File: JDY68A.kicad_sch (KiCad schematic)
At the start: 7 parts, among them U9 PAM8302AAS

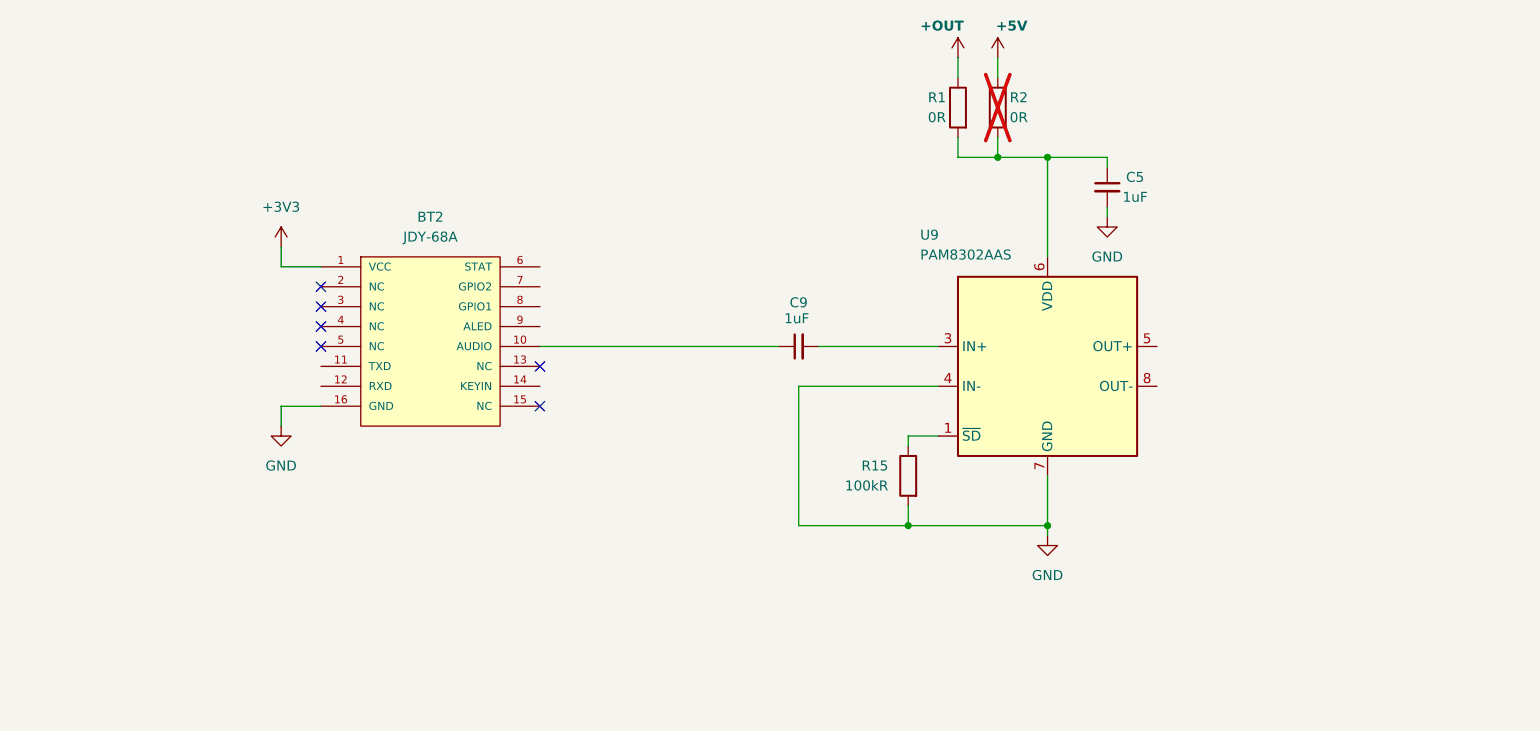
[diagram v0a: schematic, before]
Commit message: Changed LDO to Buc-Boost
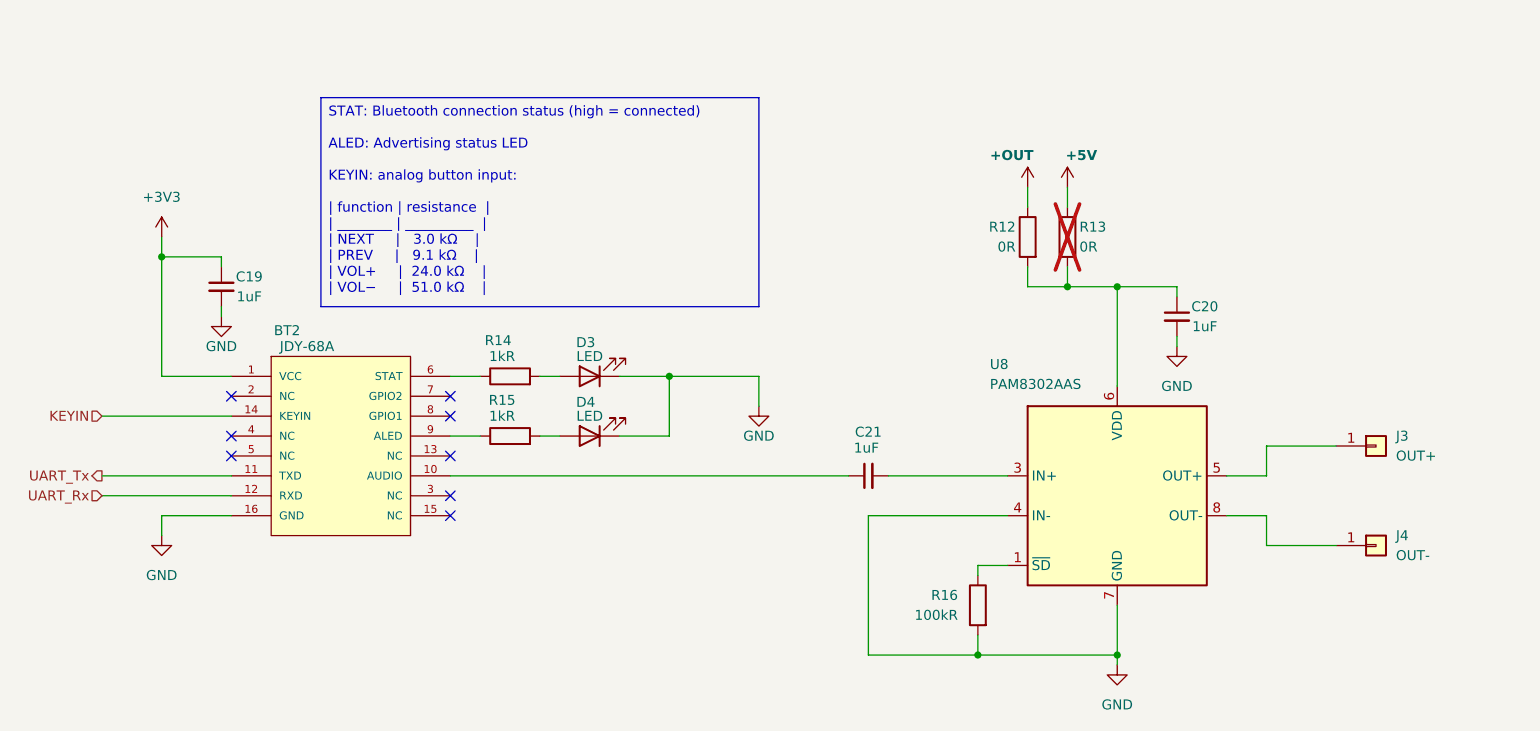
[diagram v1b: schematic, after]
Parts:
- added C19: 1uF, Capacitor_SMD:C_0805_2012Metric_Pad1.18x1.45mm_HandSolder, symbol Device:C_Small
- added D3, D4: LED, LED_SMD:LED_0805_2012Metric_Pad1.15x1.40mm_HandSolder, symbol Device:LED
- added J3: OUT+, Connector_PinSocket_2.54mm:PinSocket_1x01_P2.54mm_Vertical, symbol Connector_Generic:Conn_01x01
- added J4: OUT-, Connector_PinSocket_2.54mm:PinSocket_1x01_P2.54mm_Vertical, symbol Connector_Generic:Conn_01x01
- added R14, R15: 1kR, Resistor_SMD:R_0805_2012Metric_Pad1.20x1.40mm_HandSolder, symbol Device:R
- C20: renamed from C5; footprint (none) -> Capacitor_SMD:C_0805_2012Metric_Pad1.18x1.45mm_HandSolder
- C21: renamed from C9; footprint (none) -> Capacitor_SMD:C_0805_2012Metric_Pad1.18x1.45mm_HandSolder
- R12: renamed from R1; footprint (none) -> Resistor_SMD:R_0805_2012Metric_Pad1.20x1.40mm_HandSolder
- R13: renamed from R2; footprint (none) -> Resistor_SMD:R_0805_2012Metric_Pad1.20x1.40mm_HandSolder
- R16: renamed from R15; footprint (none) -> Resistor_SMD:R_0805_2012Metric_Pad1.20x1.40mm_HandSolder
- renumbered U9 to U8
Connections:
- net +3V3: now also C19.1
- net GND: now also C19.2, D3.1 (K), D4.1 (K)
- net at U8.5 (OUT+): now also J3.1 (Pin_1)
- net at U8.8 (OUT-): now also J4.1 (Pin_1)
- net UART_Tx: now reaches BT2.11 (TXD)
- net UART_Rx: now reaches BT2.12 (RXD)
- net KEYIN: now reaches BT2.14 (KEYIN)
- net at BT2.6 (STAT): now also R14.1
- net at BT2.9 (ALED): now also R15.1
- new net: D4.2 (A), R15.2
- new net: D3.2 (A), R14.2
- no-connect marks 6 -> 8
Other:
- moved on the sheet: BT2, C20, C21, R12, R13, R16, U8

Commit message: Added LEDs + TPs
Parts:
- BT2: footprint (none) -> JDY68A:JDY-68A_Module
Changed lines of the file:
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@@
 			)
 		)
-		(property "Footprint" ""
+		(property "Footprint" "JDY68A:JDY-68A_Module"
 			(at 91.44 78.74 0)
 			(effects

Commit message: Added layout
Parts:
- added C25: 10uF, Capacitor_SMD:C_0805_2012Metric_Pad1.18x1.45mm_HandSolder, symbol Device:C_Small
- added R24, R25: 10kR, Resistor_SMD:R_0805_2012Metric_Pad1.20x1.40mm_HandSolder, symbol Device:R
- added R26: 100kR, Resistor_SMD:R_0805_2012Metric_Pad1.20x1.40mm_HandSolder, symbol Device:R
- C21: value 1uF -> 10uF
- J3, J4: footprint Connector_PinSocket_2.54mm:PinSocket_1x01_P2.54mm_Vertical -> Connector_PinHeader_2.54mm:PinHeader_1x01_P2.54mm_Vertical
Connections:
- net GND: now also R26.1
- net at U8.3 (IN+): now also R24.2, R25.2, R26.2; no longer C21.2
- new net: C25.2, R25.1
- new net: C21.2, R24.1
- new net MCU_AUDIO: C25.1
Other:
- moved on the sheet: C21

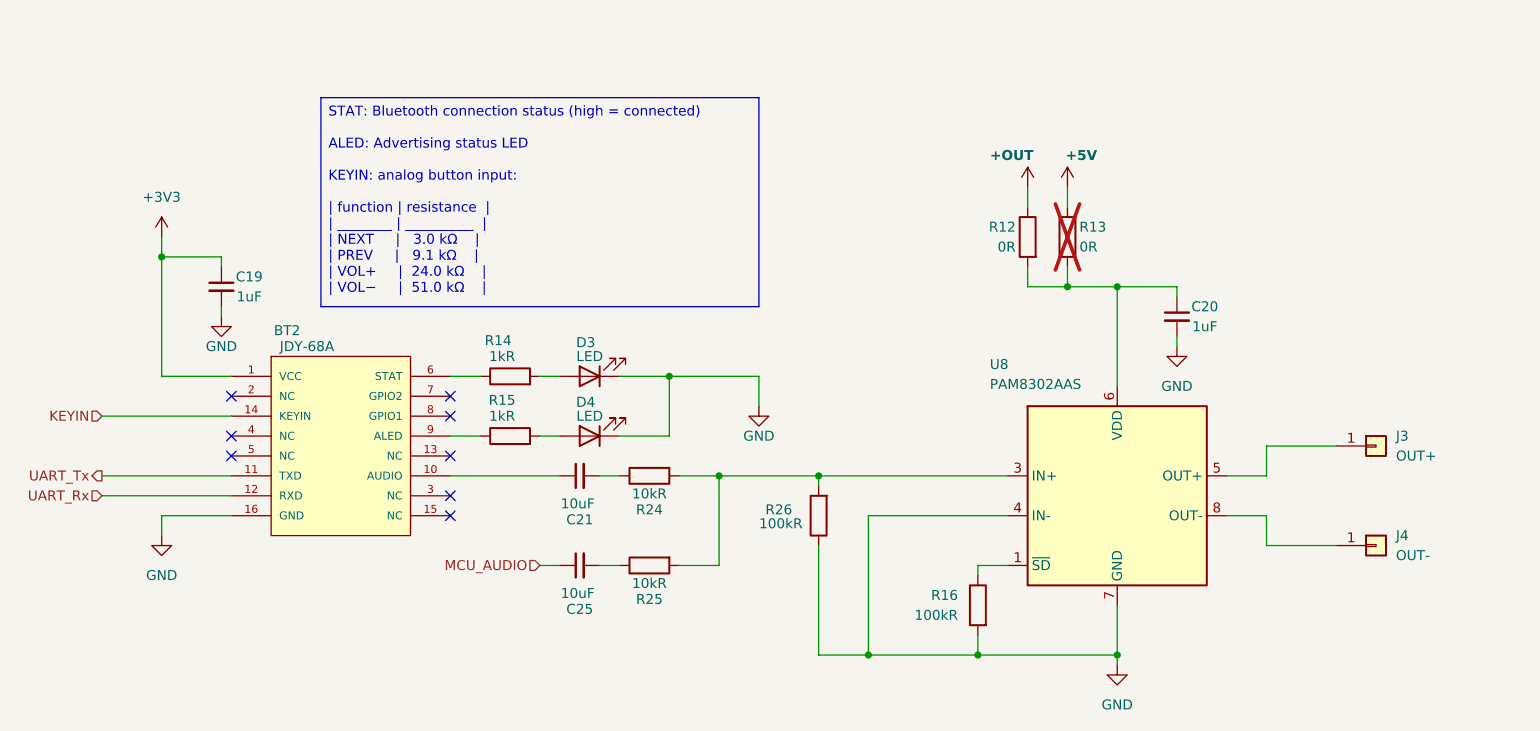
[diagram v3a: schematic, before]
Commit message: Did Silkscreen + added images of PCBA
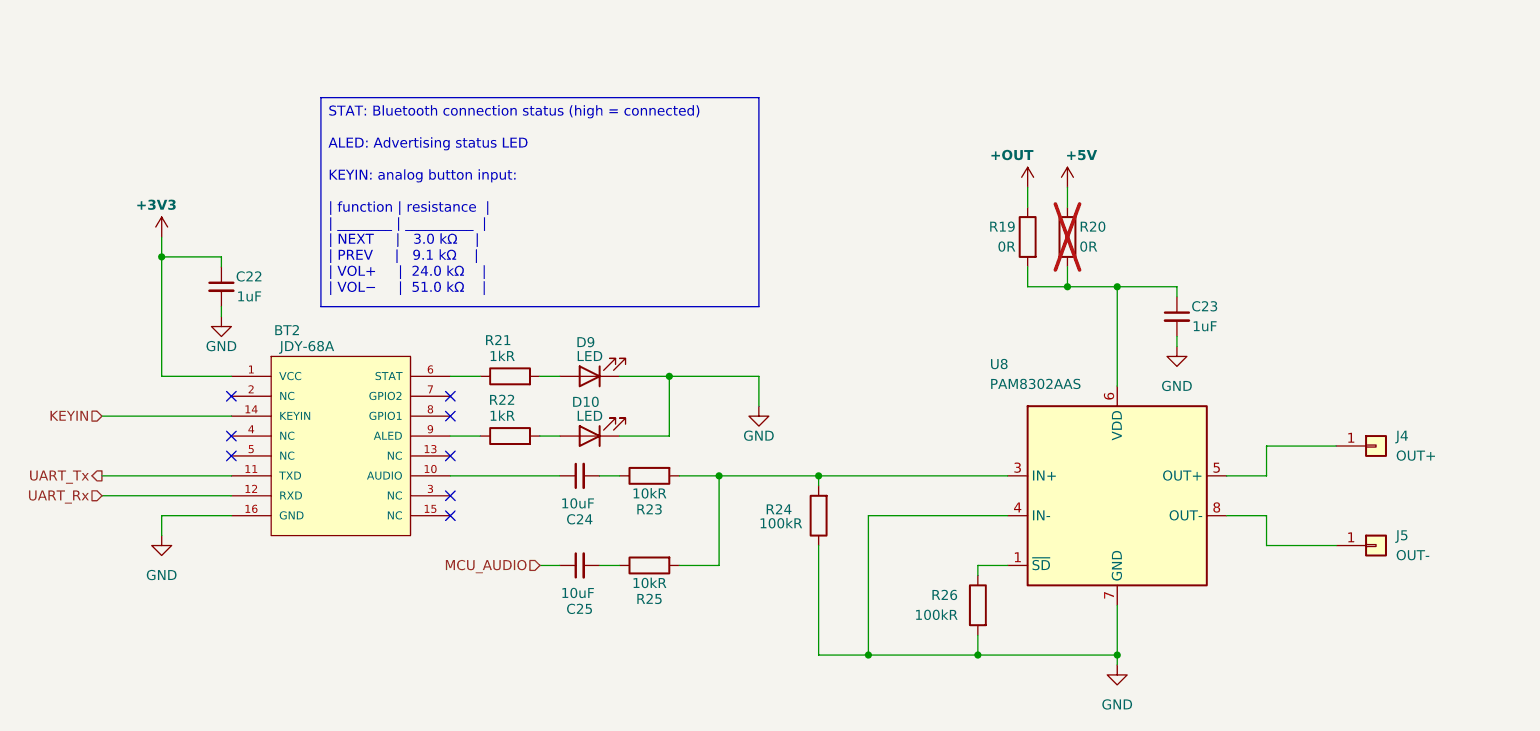
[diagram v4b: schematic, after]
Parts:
- renumbered C19 to C22, C20 to C23, C21 to C24, D4 to D10, D3 to D9, J3 to J4, J4 to J5, R12 to R19, R13 to R20, R14 to R21, R15 to R22, R24 to R23, R26 to R24, R16 to R26
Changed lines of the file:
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@@
 	(title_block
 		(title "Snail v1")
-		(date "2026-03-29")
+		(date "2026-04-06")
 		(company "Author: Christian R")
 	)
@@
 		(on_board yes)
 		(dnp no)
-		(property "Reference" "R15"
+		(property "Reference" "R22"
 			(at 112.014 83.058 90)
 			(effects
@@
 			(project "Snail_v1"
 				(path "/98695d9f-8521-4f7d-bb41-f22c1215a8e7/d0e1ba84-93bf-4c92-b310-ee99f2c34828"
-					(reference "R15")
+					(reference "R22")
 					(unit 1)
 				)
@@
 		(dnp no)
 		(fields_autoplaced yes)
-		(property "Reference" "#PWR032"
+		(property "Reference" "#PWR044"
 			(at 198.12 82.55 0)
 			(effects
@@
 			(project "Snail_v1"
 				(path "/98695d9f-8521-4f7d-bb41-f22c1215a8e7/d0e1ba84-93bf-4c92-b310-ee99f2c34828"
-					(reference "#PWR032")
+					(reference "#PWR044")
 					(unit 1)
 				)
@@
 		(on_board yes)
 		(dnp no)
-		(property "Reference" "#PWR031"
+		(property "Reference" "#PWR043"
 			(at 76.2 78.74 0)
 			(effects
@@
 			(project "Snail_v1"
 				(path "/98695d9f-8521-4f7d-bb41-f22c1215a8e7/d0e1ba84-93bf-4c92-b310-ee99f2c34828"
-					(reference "#PWR031")
+					(reference "#PWR043")
 					(unit 1)
 				)
@@
 		(on_board yes)
 		(dnp no)
-		(property "Reference" "D3"
+		(property "Reference" "D9"
 			(at 122.682 75.692 0)
 			(effects
@@
 			(project ""
 				(path "/98695d9f-8521-4f7d-bb41-f22c1215a8e7/d0e1ba84-93bf-4c92-b310-ee99f2c34828"
-					(reference "D3")
+					(reference "D9")
 					(unit 1)
 				)
@@
 		(on_board yes)
 		(dnp no)
-		(property "Reference" "D4"
+		(property "Reference" "D10"
 			(at 122.682 83.312 0)
 			(effects
@@
 			(project "Snail_v1"
 				(path "/98695d9f-8521-4f7d-bb41-f22c1215a8e7/d0e1ba84-93bf-4c92-b310-ee99f2c34828"
-					(reference "D4")
+					(reference "D10")
 					(unit 1)
 				)
@@
 		(on_board yes)
 		(dnp no)
-		(property "Reference" "R14"
+		(property "Reference" "R21"
 			(at 111.506 75.438 90)
 			(effects
@@
 			(project ""
 				(path "/98695d9f-8521-4f7d-bb41-f22c1215a8e7/d0e1ba84-93bf-4c92-b310-ee99f2c34828"
-					(reference "R14")
+					(reference "R21")
 					(unit 1)
 				)
@@
 		(on_board yes)
 		(dnp no)
-		(property "Reference" "C20"
+		(property "Reference" "C23"
 			(at 201.676 71.12 0)
 			(effects
@@
 			(project "Snail_v1"
 				(path "/98695d9f-8521-4f7d-bb41-f22c1215a8e7/d0e1ba84-93bf-4c92-b310-ee99f2c34828"
-					(reference "C20")
+					(reference "C23")
 					(unit 1)
 				)
@@
 		(on_board yes)
 		(dnp no)
-		(property "Reference" "R24"
+		(property "Reference" "R23"
 			(at 130.81 97.028 90)
 			(effects
@@
 			(project "Snail_v1"
 				(path "/98695d9f-8521-4f7d-bb41-f22c1215a8e7/d0e1ba84-93bf-4c92-b310-ee99f2c34828"
-					(reference "R24")
+					(reference "R23")
 					(unit 1)
 				)
@@
 		(on_board yes)
 		(dnp no)
-		(property "Reference" "#PWR029"
+		(property "Reference" "#PWR041"
 			(at 184.15 59.69 0)
 			(effects
@@
 			(project "Snail_v1"
 				(path "/98695d9f-8521-4f7d-bb41-f22c1215a8e7/d0e1ba84-93bf-4c92-b310-ee99f2c34828"
-					(reference "#PWR029")
+					(reference "#PWR041")
 					(unit 1)
 				)
@@
 		(on_board yes)
 		(dnp no)
-		(property "Reference" "R26"
+		(property "Reference" "R24"
 			(at 147.32 97.028 0)
 			(effects
@@
 			(project "Snail_v1"
 				(path "/98695d9f-8521-4f7d-bb41-f22c1215a8e7/d0e1ba84-93bf-4c92-b310-ee99f2c34828"
-					(reference "R26")
+					(reference "R24")
 					(unit 1)
 				)
@@
 		(dnp no)
 		(fields_autoplaced yes)
-		(property "Reference" "J3"
+		(property "Reference" "J4"
 			(at 226.06 87.6299 0)
 			(effects
@@
 			(project ""
 				(path "/98695d9f-8521-4f7d-bb41-f22c1215a8e7/d0e1ba84-93bf-4c92-b310-ee99f2c34828"
-					(reference "J3")
+					(reference "J4")
 					(unit 1)
 				)
@@
 		(on_board yes)
 		(dnp no)
-		(property "Reference" "C19"
+		(property "Reference" "C22"
 			(at 79.756 67.31 0)
 			(effects
@@
 			(project "Snail_v1"
 				(path "/98695d9f-8521-4f7d-bb41-f22c1215a8e7/d0e1ba84-93bf-4c92-b310-ee99f2c34828"
-					(reference "C19")
+					(reference "C22")
 					(unit 1)
 				)
@@
 		(on_board yes)
 		(dnp no)
-		(fields_autoplaced yes)
-		(property "Reference" "#PWR030"
+		(property "Reference" "#PWR042"
 			(at 68.58 66.04 0)
 			(effects
@@
 		)
 		(property "Value" "+3V3"
-			(at 68.58 57.15 0)
-			(effects
-				(font
-					(size 1.27 1.27)
-				)
+			(at 65.278 58.166 0)
+			(effects
+				(font
+					(size 1.27 1.27)
+					(thickness 0.254)
+					(bold yes)
+					(color 255 0 0 1)
+				)
+				(justify left)
 			)
 		)
@@
 			(project ""
 				(path "/98695d9f-8521-4f7d-bb41-f22c1215a8e7/d0e1ba84-93bf-4c92-b310-ee99f2c34828"
-					(reference "#PWR030")
+					(reference "#PWR042")
 					(unit 1)
 				)
@@
 		(on_board yes)
 		(dnp no)
-		(property "Reference" "R12"
+		(property "Reference" "R19"
 			(at 177.546 60.96 0)
 			(effects
@@
 			(project "Snail_v1"
 				(path "/98695d9f-8521-4f7d-bb41-f22c1215a8e7/d0e1ba84-93bf-4c92-b310-ee99f2c34828"
-					(reference "R12")
+					(reference "R19")
 					(unit 1)
 				)
@@
 		(on_board yes)
 		(dnp no)
-		(property "Reference" "R16"
+		(property "Reference" "R26"
 			(at 170.18 107.9499 0)
 			(effects
@@
 			(project "Snail_v1"
 				(path "/98695d9f-8521-4f7d-bb41-f22c1215a8e7/d0e1ba84-93bf-4c92-b310-ee99f2c34828"
-					(reference "R16")
+					(reference "R26")
 					(unit 1)
 				)
@@
 		(on_board yes)
 		(dnp yes)
-		(property "Reference" "R13"
+		(property "Reference" "R20"
 			(at 185.674 60.96 0)
 			(effects
@@
 			(project "Snail_v1"
 				(path "/98695d9f-8521-4f7d-bb41-f22c1215a8e7/d0e1ba84-93bf-4c92-b310-ee99f2c34828"
-					(reference "R13")
+					(reference "R20")
 					(unit 1)
 				)
@@
 		(dnp no)
 		(fields_autoplaced yes)
-		(property "Reference" "#PWR035"
+		(property "Reference" "#PWR047"
 			(at 190.5 123.19 0)
 			(effects
@@
 			(project "Snail_v1"
 				(path "/98695d9f-8521-4f7d-bb41-f22c1215a8e7/d0e1ba84-93bf-4c92-b310-ee99f2c34828"
-					(reference "#PWR035")
+					(reference "#PWR047")
 					(unit 1)
 				)
@@
 		(dnp no)
 		(fields_autoplaced yes)
-		(property "Reference" "J4"
+		(property "Reference" "J5"
 			(at 226.06 100.3299 0)
 			(effects
@@
 			(project "Snail_v1"
 				(path "/98695d9f-8521-4f7d-bb41-f22c1215a8e7/d0e1ba84-93bf-4c92-b310-ee99f2c34828"
-					(reference "J4")
+					(reference "J5")
 					(unit 1)
 				)
@@
 		(dnp no)
 		(fields_autoplaced yes)
-		(property "Reference" "#PWR034"
+		(property "Reference" "#PWR046"
 			(at 68.58 106.68 0)
 			(effects
@@
 			(project ""
 				(path "/98695d9f-8521-4f7d-bb41-f22c1215a8e7/d0e1ba84-93bf-4c92-b310-ee99f2c34828"
-					(reference "#PWR034")
+					(reference "#PWR046")
 					(unit 1)
 				)
@@
 		(on_board yes)
 		(dnp no)
-		(property "Reference" "#PWR028"
+		(property "Reference" "#PWR040"
 			(at 179.07 59.69 0)
 			(effects
@@
 			(project "Snail_v1"
 				(path "/98695d9f-8521-4f7d-bb41-f22c1215a8e7/d0e1ba84-93bf-4c92-b310-ee99f2c34828"
-					(reference "#PWR028")
+					(reference "#PWR040")
 					(unit 1)
 				)
@@
 		(on_board yes)
 		(dnp no)
-		(property "Reference" "#PWR033"
+		(property "Reference" "#PWR045"
 			(at 144.78 90.17 0)
 			(effects
@@
 			(project "Snail_v1"
 				(path "/98695d9f-8521-4f7d-bb41-f22c1215a8e7/d0e1ba84-93bf-4c92-b310-ee99f2c34828"
-					(reference "#PWR033")
+					(reference "#PWR045")
 					(unit 1)
 				)
@@
 		(on_board yes)
 		(dnp no)
-		(property "Reference" "C21"
+		(property "Reference" "C24"
 			(at 121.92 98.298 90)
 			(effects
@@
 			(project "Snail_v1"
 				(path "/98695d9f-8521-4f7d-bb41-f22c1215a8e7/d0e1ba84-93bf-4c92-b310-ee99f2c34828"
-					(reference "C21")
-					(unit 1)
-				)
+					(reference "C24")
+					(unit 1)
+				)

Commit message: Added missing AMP_nSD connection to MCU via 5V_EN
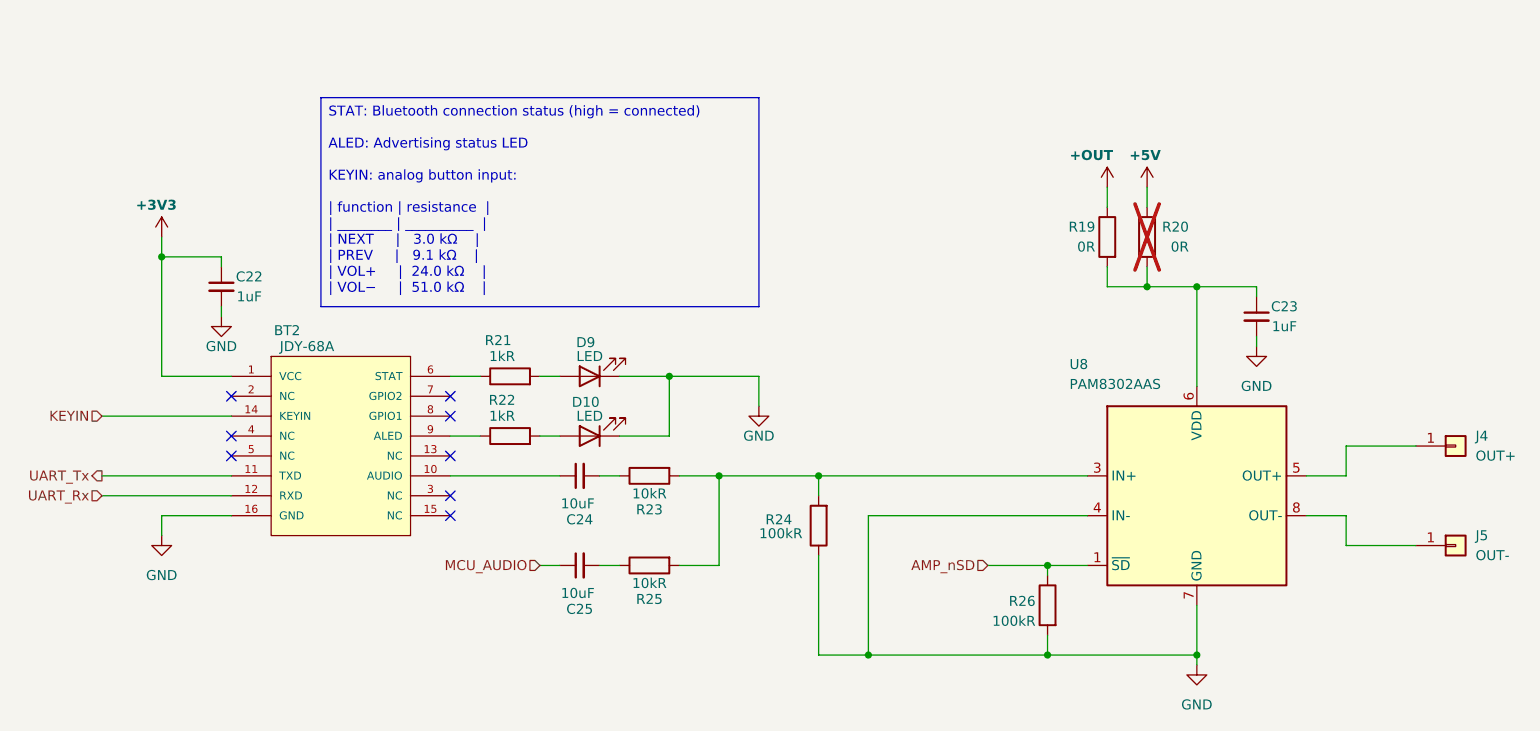
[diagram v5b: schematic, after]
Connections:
- net AMP_nSD: now reaches R26.1, U8.1 (~{SD})
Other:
- moved on the sheet: C23, J4, J5, R19, R20, R24, R26, U8

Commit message: Changed layout + added dimensions
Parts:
- J4, J5: footprint Connector_PinHeader_2.54mm:PinHeader_1x01_P2.54mm_Vertical -> Connector_Wire:SolderWirePad_1x01_SMD_1.5x3mm
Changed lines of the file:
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@@
 			)
 		)
-		(property "Footprint" "Connector_PinHeader_2.54mm:PinHeader_1x01_P2.54mm_Vertical"
+		(property "Footprint" "Connector_Wire:SolderWirePad_1x01_SMD_1.5x3mm"
 			(at 233.68 88.9 0)
 			(effects
@@
 			)
 		)
-		(property "Footprint" "Connector_PinHeader_2.54mm:PinHeader_1x01_P2.54mm_Vertical"
+		(property "Footprint" "Connector_Wire:SolderWirePad_1x01_SMD_1.5x3mm"
 			(at 233.68 101.6 0)
 			(effects
